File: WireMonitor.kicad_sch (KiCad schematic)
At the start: 4 parts, among them J1 2191160161, U1 INA4180A1, U2 INA4180A1, U3 INA4180A1

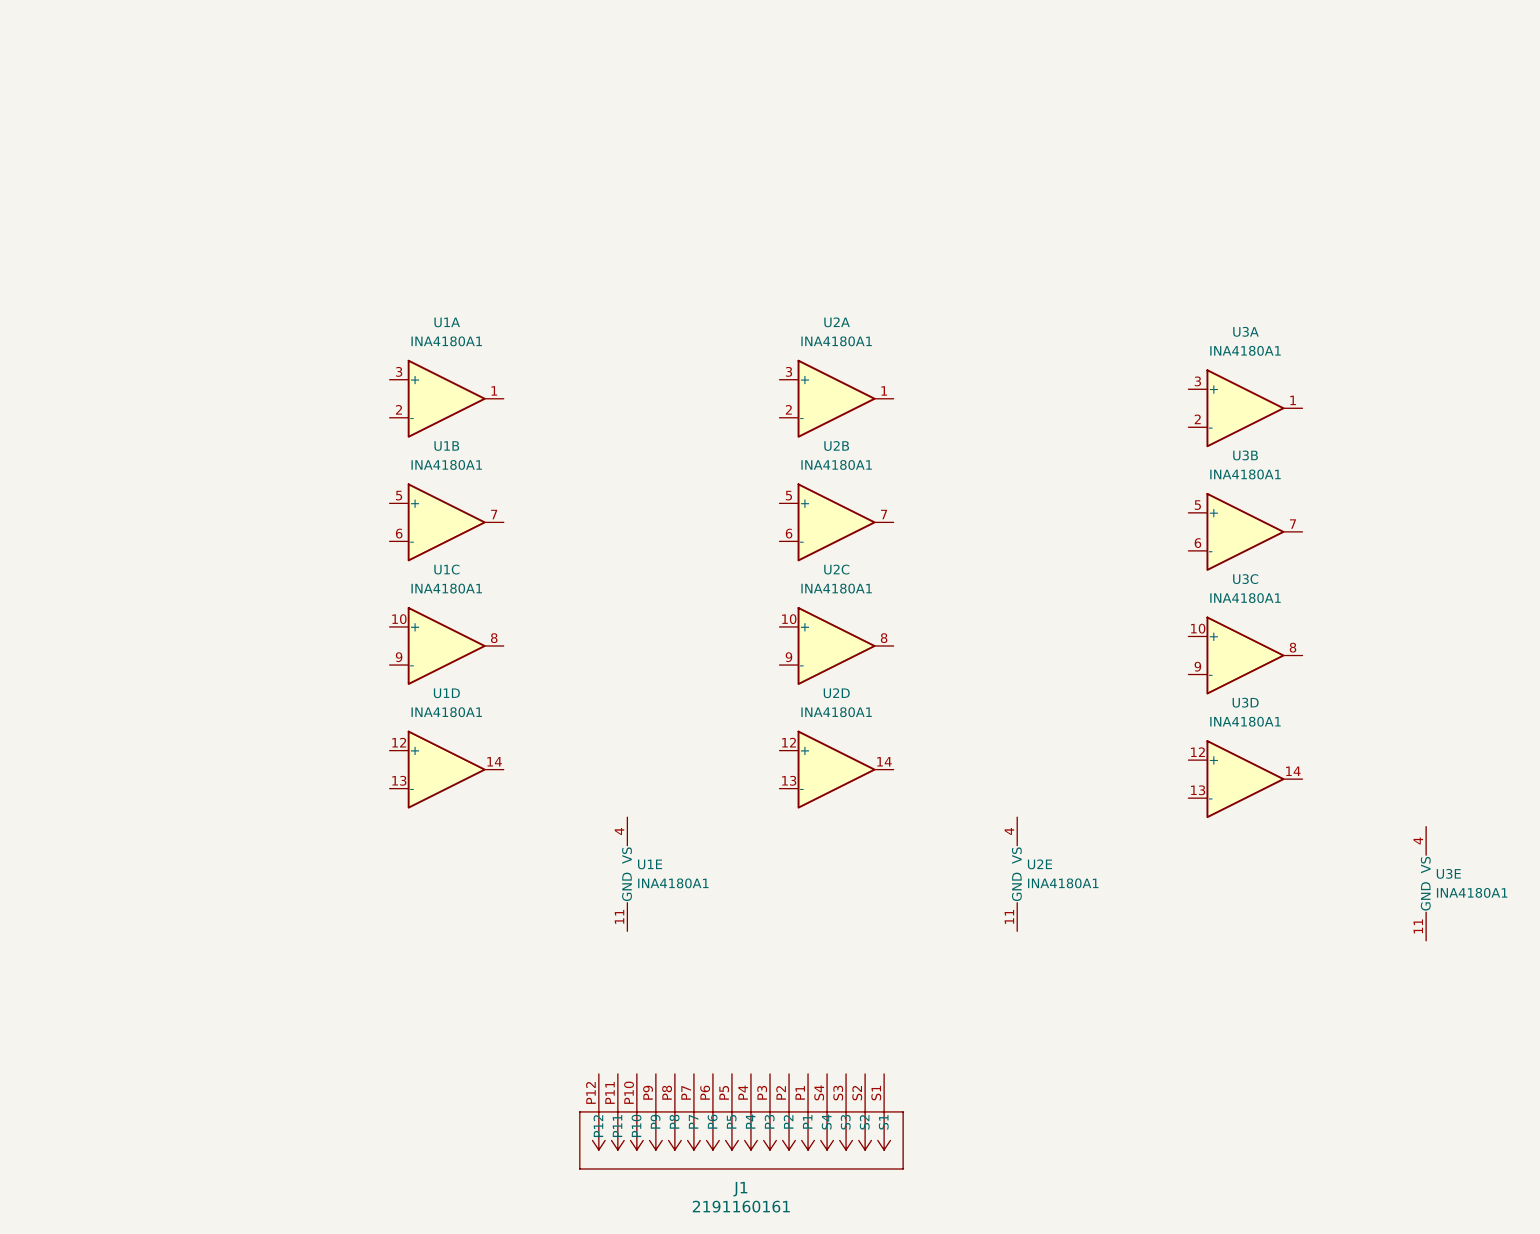
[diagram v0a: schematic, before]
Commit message: Added INA302
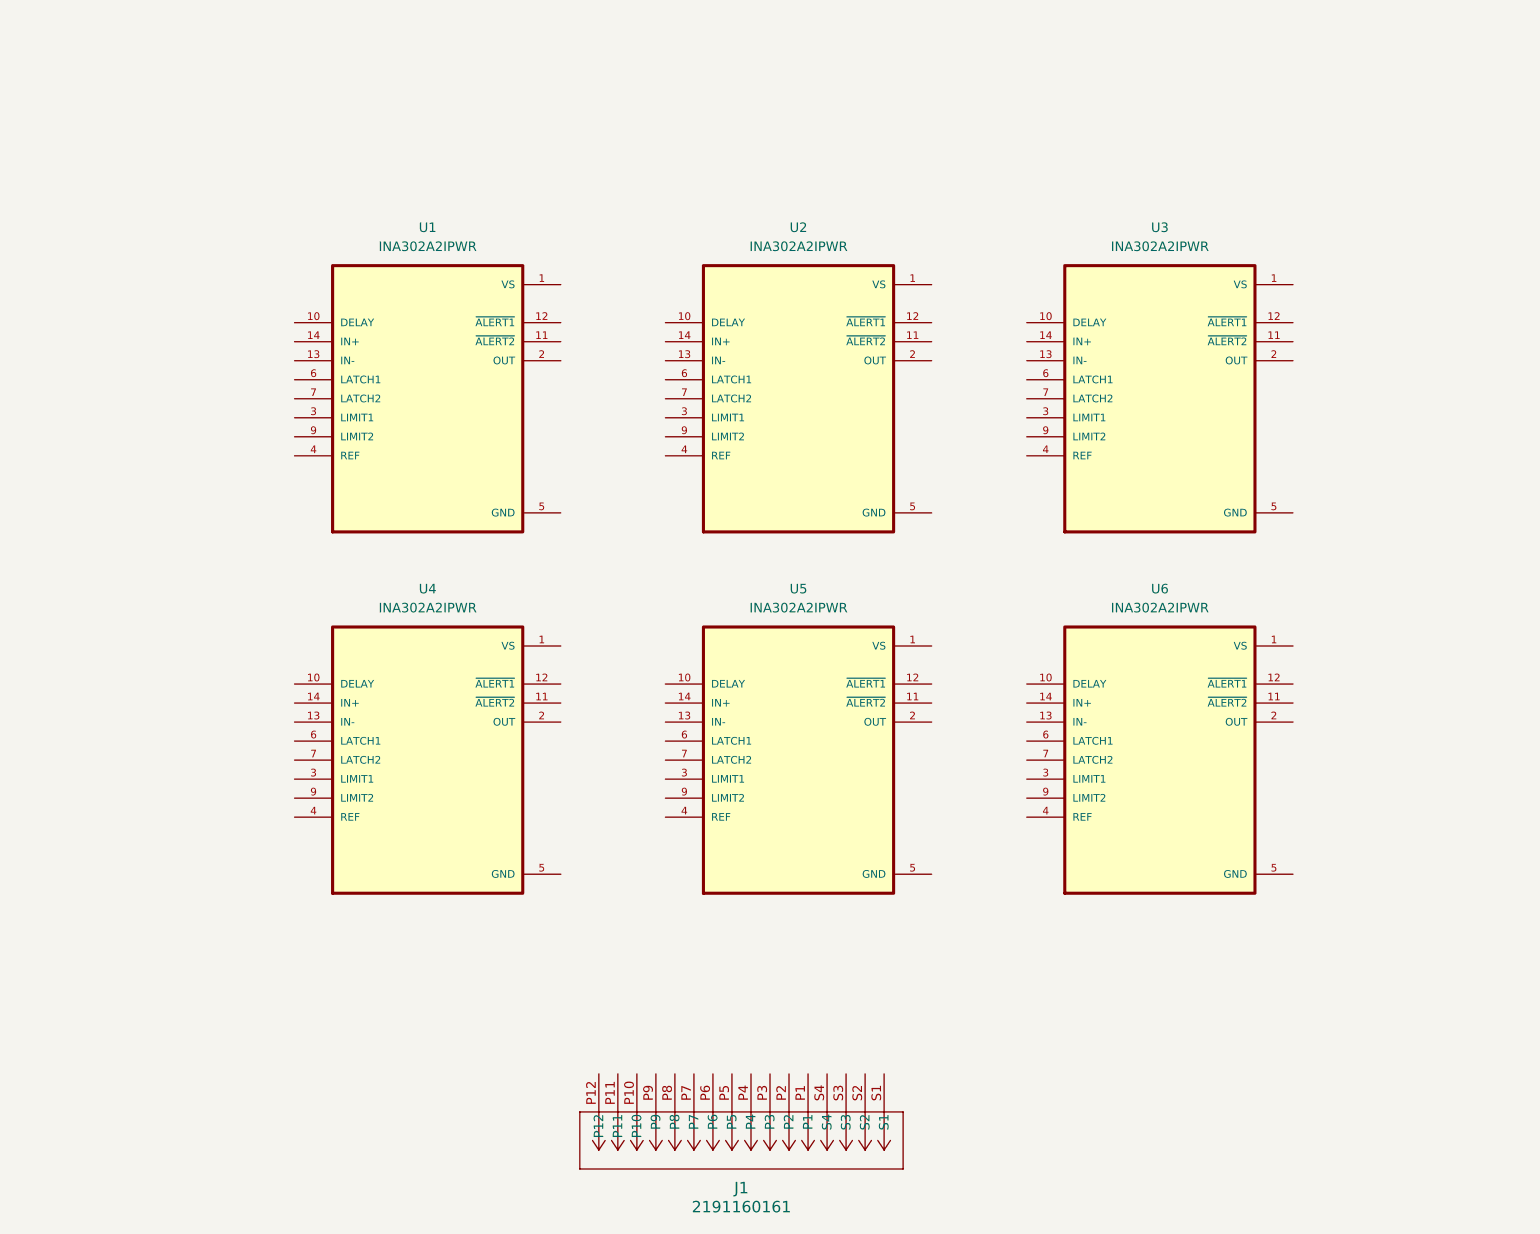
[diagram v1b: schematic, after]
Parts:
- removed U1, U2, U3: INA4180A1, Package_SO:TSSOP-14_4.4x5mm_P0.65mm, symbol Amplifier_Current:INA4180A1
- added U1, U2, U3, U4, U5, U6: INA302A2IPWR, INA302A2IPWR:SOP65P640X120-14N, symbol INA302A2IPWR:INA302A2IPWR

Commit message: schematic
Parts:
- removed U2, U3, U4, U5, U6: INA302A2IPWR, INA302A2IPWR:SOP65P640X120-14N, symbol INA302A2IPWR:INA302A2IPWR
- added C_BLK1: 1uF, symbol Device:C
- added C_BP1: 0.1uF, symbol Device:C
- added C_DELAY1: 4.7nF, symbol Device:C
- added R_L1: 13k, symbol Device:R_US
- added R_L2: 11.8k, symbol Device:R_US
- added R_P1, R_P2: 4.7, symbol Device:R_US
- added R_PU1, R_PU2: 10k, symbol Device:R_US
- added R_S1: 2m, symbol Device:R_US
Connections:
- net at U1.1 (VS): now also C_BLK1.2, C_BP1.2, R_PU1.1, R_PU2.2
- net at U1.10 (DELAY): now also C_DELAY1.1
- net at U1.11 (~{ALERT2}): now also R_PU2.1
- net at U1.12 (~{ALERT1}): now also R_PU1.2
- net at U1.13 (IN-): now also R_P2.1
- net at U1.14 (IN+): now also R_P1.2
- net at U1.3 (LIMIT1): now also R_L1.1
- net at U1.4 (REF): now also U1.5 (GND), U1.6 (LATCH1), U1.7 (LATCH2), C_DELAY1.2, R_L1.2, R_L2.1
- net at U1.9 (LIMIT2): now also R_L2.2
- net L1: now reaches J1.P1
- net L1: now also R_P2.2, R_S1.2
- net L2: now reaches J1.P2
- net L3: now reaches J1.P3
- net L4: now reaches J1.P4
- net L5: now reaches J1.P5
- net L6: now reaches J1.P6
- new net GND: C_BLK1.1, C_BP1.1
- new net PS_12V_1: R_P1.1, R_S1.1
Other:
- moved on the sheet: J1, U1
